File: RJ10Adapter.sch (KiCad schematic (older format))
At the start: 10 parts, among them J1 RJ10, J2 Conn_01x06_Male, J3 USB_B_Micro, SW1 SW_Push, U1 AMS1117-3.3, U2 ESP-12F

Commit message: Resistor to GPIO
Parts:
- added R3: R, Resistor_SMD:R_0805_2012Metric_Pad1.15x1.40mm_HandSolder, symbol Device:R
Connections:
- net Vin: now also R3.1; no longer U2.17 (GPIO2)
- new net: R3.2, U2.17 (GPIO2)
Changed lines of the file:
@@
 Sheet 1 1
 Title "RJ FTDI Adapter"
-Date "2019-04-20"
-Rev "1.1"
+Date "2019-05-01"
+Rev "1.2"
 Comp "haus-automatisierung.com"
 Comment1 "Matthias Kleine"
@@
 Wire Wire Line
 	5150 1600 5450 1600
-Wire Wire Line
-	5450 1600 5450 800
-Wire Wire Line
-	5450 800  4550 800
 Connection ~ 4550 800
 Wire Wire Line
@@
 	5800 2900 4550 2900
 Connection ~ 4550 2900
-Connection ~ 5450 800
 Wire Wire Line
 	5300 3500 5300 3150
@@
 Wire Wire Line
 	5100 3700 5450 3700
-Wire Wire Line
-	5450 800  7400 800
 Wire Wire Line
 	5150 1700 6350 1700
@@
 Text Label 4850 3600 0    50   ~ 0
 TX
+Wire Wire Line
+	4550 800  5450 800
+$Comp
+L Device:R R3
+U 1 1 5CC9A463
+P 5450 1000
+F 0 "R3" H 5520 1046 50  0000 L CNN
+F 1 "R" H 5520 955 50  0000 L CNN
+F 2 "Resistor_SMD:R_0805_2012Metric_Pad1.15x1.40mm_HandSolder" V 5380 1000 50  0001 C CNN
+F 3 "~" H 5450 1000 50  0001 C CNN
+	1    5450 1000
+	1    0    0    -1
+$EndComp
+Wire Wire Line
+	5450 850  5450 800
+Connection ~ 5450 800
+Wire Wire Line
+	5450 800  7400 800
+Wire Wire Line
+	5450 1600 5450 1150
 $EndSCHEMATC

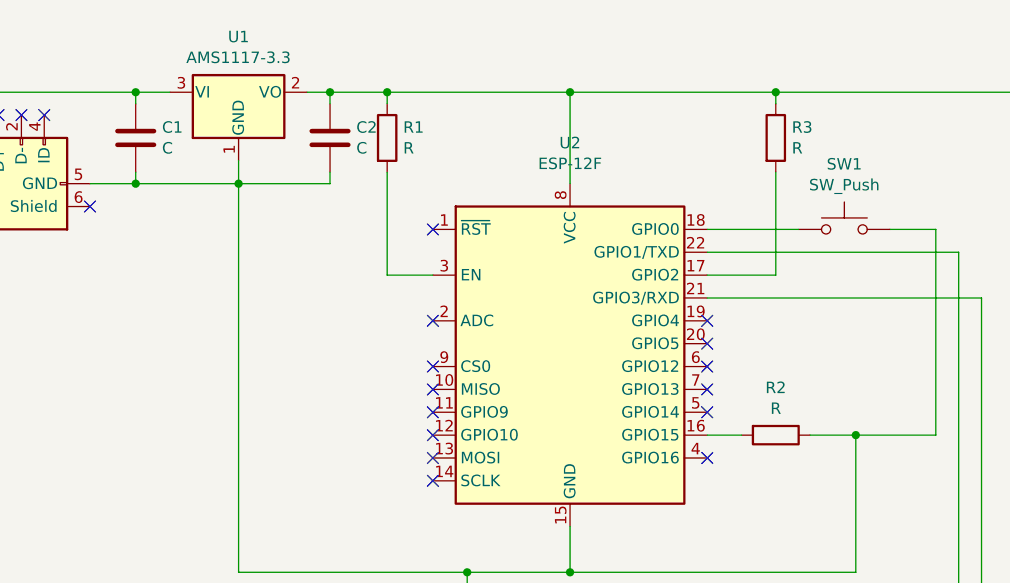
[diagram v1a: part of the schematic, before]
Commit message: added resistor
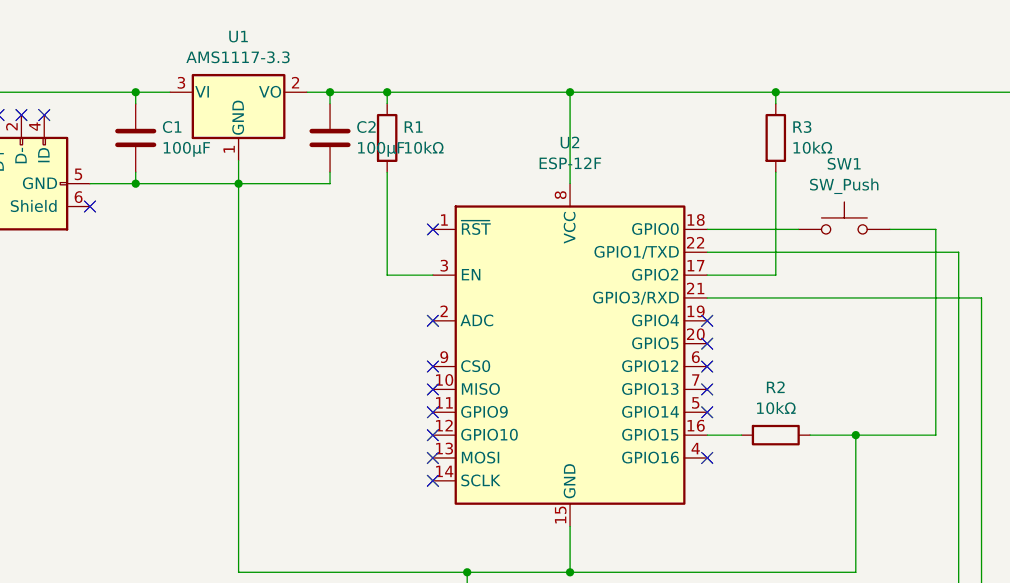
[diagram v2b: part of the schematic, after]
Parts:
- C1, C2: value C -> 100µF
- J1: footprint libs:MEBP_44S_MK -> halibs:MEBP_44S
- R1, R2, R3: value R -> 10kΩ
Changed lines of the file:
@@
 Sheet 1 1
 Title "RJ FTDI Adapter"
-Date "2019-05-01"
+Date "2019-05-11"
 Rev "1.2"
 Comp "haus-automatisierung.com"
@@
 F 0 "J1" H 3400 4150 50  0000 C CNN
 F 1 "RJ10" H 3850 4150 50  0000 C CNN
-F 2 "libs:MEBP_44S_MK" V 3650 3850 50  0001 C CNN
+F 2 "halibs:MEBP_44S" V 3650 3850 50  0001 C CNN
 F 3 "~" V 3650 3850 50  0001 C CNN
 	1    3650 3800
@@
 P 5450 2300
 F 0 "R2" V 5243 2300 50  0000 C CNN
-F 1 "R" V 5334 2300 50  0000 C CNN
+F 1 "10kΩ" V 5334 2300 50  0000 C CNN
 F 2 "Resistor_SMD:R_0805_2012Metric_Pad1.15x1.40mm_HandSolder" V 5380 2300 50  0001 C CNN
 F 3 "~" H 5450 2300 50  0001 C CNN
@@
 P 2650 1000
 F 0 "C1" H 2765 1046 50  0000 L CNN
-F 1 "C" H 2765 955 50  0000 L CNN
+F 1 "100µF" H 2765 955 50  0000 L CNN
 F 2 "Capacitor_SMD:C_0805_2012Metric_Pad1.15x1.40mm_HandSolder" H 2688 850 50  0001 C CNN
 F 3 "~" H 2650 1000 50  0001 C CNN
@@
 P 3500 1000
 F 0 "C2" H 3615 1046 50  0000 L CNN
-F 1 "C" H 3615 955 50  0000 L CNN
+F 1 "100µF" H 3615 955 50  0000 L CNN
 F 2 "Capacitor_SMD:C_0805_2012Metric_Pad1.15x1.40mm_HandSolder" H 3538 850 50  0001 C CNN
 F 3 "~" H 3500 1000 50  0001 C CNN
@@
 P 3750 1000
 F 0 "R1" H 3820 1046 50  0000 L CNN
-F 1 "R" H 3820 955 50  0000 L CNN
+F 1 "10kΩ" H 3820 955 50  0000 L CNN
 F 2 "Resistor_SMD:R_0805_2012Metric_Pad1.15x1.40mm_HandSolder" V 3680 1000 50  0001 C CNN
 F 3 "~" H 3750 1000 50  0001 C CNN
@@
 P 5450 1000
 F 0 "R3" H 5520 1046 50  0000 L CNN
-F 1 "R" H 5520 955 50  0000 L CNN
+F 1 "10kΩ" H 5520 955 50  0000 L CNN
 F 2 "Resistor_SMD:R_0805_2012Metric_Pad1.15x1.40mm_HandSolder" V 5380 1000 50  0001 C CNN
 F 3 "~" H 5450 1000 50  0001 C CNN
